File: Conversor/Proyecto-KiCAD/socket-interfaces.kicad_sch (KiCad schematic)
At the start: 24 parts, among them J10 DIMM100, P10 Header GPIO, P11 Header SD, P5 Header 7X2, P6 Header UART, P7 Header I2C, P8 Header PWM, P9 Header ADC, SW1 Switch, SW2 Switch, SW3 Switch, SW4 Switch

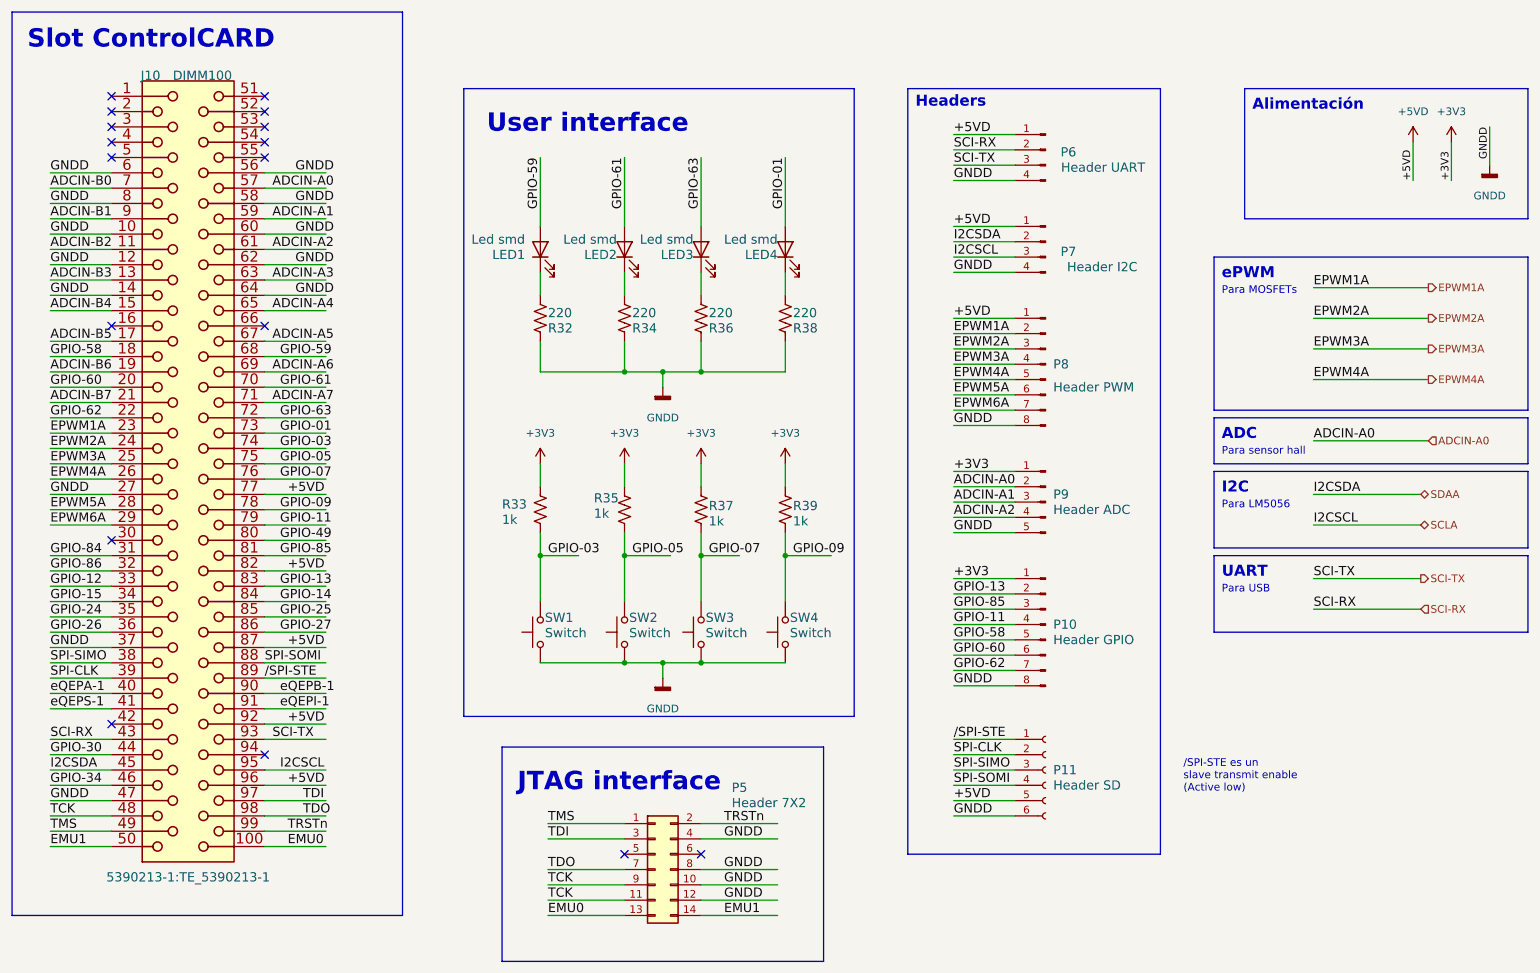
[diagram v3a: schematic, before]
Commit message: Arreglar los primeros dos items marcados por Jorge
- Usar EPWM1A/B y EPWM2A/B para poder usar la función de phase-shift de
los modulos PWM y ahorrarse la sincronización manual
- Agregar diodos de descarga D8 y D9 a la salida de los drivers
- Agregar el Technical Reference Manual del DSP a la bibliografía
(descripción ultra detallada de todas las funciones del DSP)
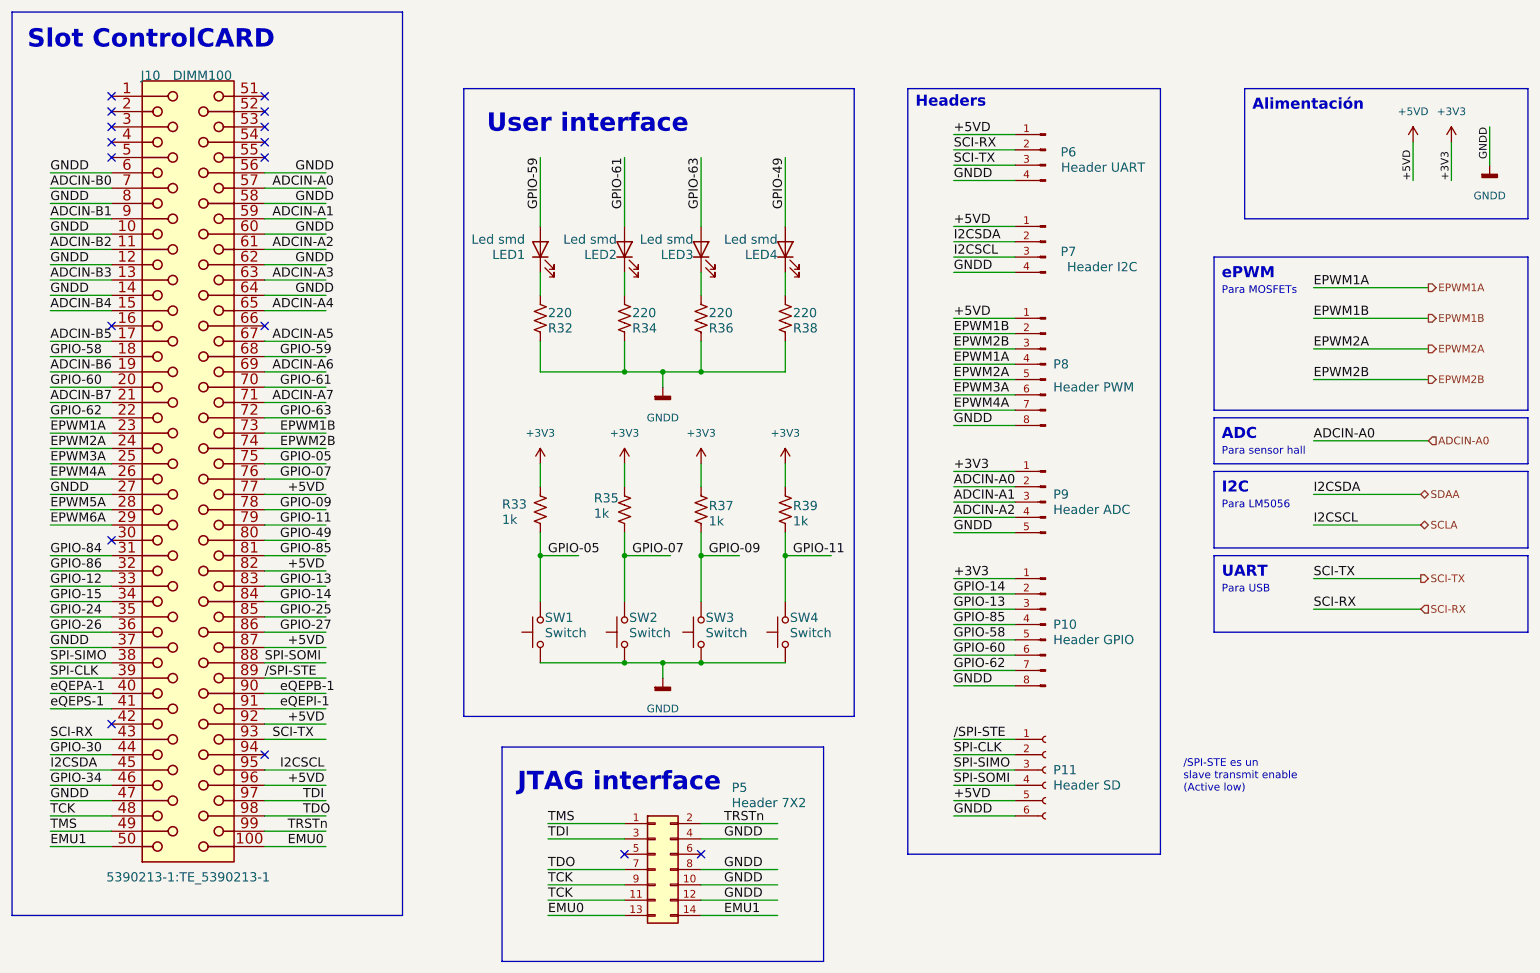
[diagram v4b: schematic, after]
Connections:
- net EPWM1A: now also P8.4 (Pin_4); no longer P8.2 (Pin_2)
- net EPWM2A: now also P8.5 (Pin_5); no longer P8.3 (Pin_3)
- net EPWM3A: now also P8.6 (Pin_6); no longer P8.4 (Pin_4)
- net EPWM4A: now also P8.7 (Pin_7); no longer P8.5 (Pin_5)
- net EPWM5A: no longer P8.6 (Pin_6)
- net EPWM6A: no longer P8.7 (Pin_7)
- net GPIO-05: now also R33.1, SW1.2; no longer R35.1, SW2.2
- net GPIO-07: now also R35.1, SW2.2; no longer R37.1, SW3.2
- net GPIO-09: now also R37.1, SW3.2; no longer R39.1, SW4.2
- net GPIO-11: now also R39.1, SW4.2; no longer P10.4 (Pin_4)
- net GPIO-13: now also P10.3 (Pin_3); no longer P10.2 (Pin_2)
- net GPIO-14: now also P10.2 (Pin_2)
- net GPIO-49: now also LED4.2 (A)
- net GPIO-85: now also P10.4 (Pin_4); no longer P10.3 (Pin_3)
- net GPIO-01 renamed EPWM1B
- net EPWM1B: now also P8.2 (Pin_2); no longer LED4.2 (A)
- removed net GPIO-03: J10.74 (p74), R33.1, SW1.2
- new net EPWM2B: J10.74 (p74), P8.3 (Pin_3)
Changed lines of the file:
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@@
     (effects (font (size 1.524 1.524)) (justify left bottom))
   )
-  (label "EPWM2A" (at 175.26 71.12 0)
-    (effects (font (size 1.524 1.524)) (justify left bottom))
-  )
-  (label "GPIO-11" (at 175.26 116.84 0)
+  (label "EPWM2B" (at 175.26 71.12 0)
+    (effects (font (size 1.524 1.524)) (justify left bottom))
+  )
+  (label "GPIO-85" (at 175.26 116.84 0)
     (effects (font (size 1.524 1.524)) (justify left bottom))
   )
@@
     (effects (font (size 1.524 1.524)) (justify left bottom))
   )
-  (label "EPWM5A" (at 175.26 78.74 0)
+  (label "EPWM3A" (at 175.26 78.74 0)
     (effects (font (size 1.524 1.524)) (justify left bottom))
   )
@@
     (effects (font (size 1.524 1.524)) (justify left bottom))
   )
-  (label "GPIO-85" (at 175.26 114.3 0)
+  (label "GPIO-13" (at 175.26 114.3 0)
     (effects (font (size 1.524 1.524)) (justify left bottom))
   )
@@
     (effects (font (size 1.524 1.524)) (justify left bottom))
   )
-  (label "EPWM6A" (at 175.26 81.28 0)
+  (label "EPWM4A" (at 175.26 81.28 0)
     (effects (font (size 1.524 1.524)) (justify left bottom))
   )
@@
     (effects (font (size 1.524 1.524)) (justify left bottom))
   )
-  (label "EPWM1A" (at 175.26 68.58 0)
+  (label "EPWM1B" (at 175.26 68.58 0)
     (effects (font (size 1.524 1.524)) (justify left bottom))
   )
@@
     (effects (font (size 1.524 1.524)) (justify left bottom))
   )
-  (label "GPIO-13" (at 175.26 111.76 0)
+  (label "GPIO-14" (at 175.26 111.76 0)
     (effects (font (size 1.524 1.524)) (justify left bottom))
   )
@@
     (effects (font (size 1.524 1.524)) (justify left bottom))
   )
-  (label "GPIO-05" (at 121.92 105.41 0)
+  (label "GPIO-07" (at 121.92 105.41 0)
     (effects (font (size 1.524 1.524)) (justify left bottom))
   )
@@
     (effects (font (size 1.524 1.524)) (justify left bottom))
   )
-  (label "EPWM3A" (at 175.26 73.66 0)
+  (label "EPWM1A" (at 175.26 73.66 0)
     (effects (font (size 1.524 1.524)) (justify left bottom))
   )
@@
     (effects (font (size 1.524 1.524)) (justify left bottom))
   )
-  (label "EPWM2A" (at 234.95 66.04 0)
+  (label "EPWM1B" (at 234.95 66.04 0)
     (effects (font (size 1.524 1.524)) (justify left bottom))
   )
@@
     (effects (font (size 1.524 1.524)) (justify left bottom))
   )
-  (label "GPIO-03" (at 107.95 105.41 0)
+  (label "GPIO-05" (at 107.95 105.41 0)
     (effects (font (size 1.524 1.524)) (justify left bottom))
   )
@@
     (effects (font (size 1.524 1.524)) (justify left bottom))
   )
-  (label "GPIO-03" (at 63.5 87.63 0)
+  (label "EPWM2B" (at 63.5 87.63 0)
     (effects (font (size 1.524 1.524)) (justify left bottom))
   )
@@
     (effects (font (size 1.524 1.524)) (justify left bottom))
   )
-  (label "EPWM3A" (at 234.95 71.12 0)
+  (label "EPWM2A" (at 234.95 71.12 0)
     (effects (font (size 1.524 1.524)) (justify left bottom))
   )
@@
     (effects (font (size 1.524 1.524)) (justify left bottom))
   )
-  (label "GPIO-01" (at 147.32 39.37 270)
+  (label "GPIO-49" (at 147.32 39.37 270)
     (effects (font (size 1.524 1.524)) (justify right bottom))
   )
@@
     (effects (font (size 1.524 1.524)) (justify left bottom))
   )
-  (label "EPWM4A" (at 234.95 76.2 0)
+  (label "EPWM2B" (at 234.95 76.2 0)
     (effects (font (size 1.524 1.524)) (justify left bottom))
   )
@@
     (effects (font (size 1.524 1.524)) (justify left bottom))
   )
-  (label "GPIO-01" (at 63.5 85.09 0)
+  (label "EPWM1B" (at 63.5 85.09 0)
     (effects (font (size 1.524 1.524)) (justify left bottom))
   )
@@
     (effects (font (size 1.524 1.524)) (justify left bottom))
   )
-  (label "EPWM4A" (at 175.26 76.2 0)
+  (label "EPWM2A" (at 175.26 76.2 0)
     (effects (font (size 1.524 1.524)) (justify left bottom))
   )
@@
     (effects (font (size 1.524 1.524)) (justify left bottom))
   )
-  (label "GPIO-09" (at 148.59 105.41 0)
+  (label "GPIO-11" (at 148.59 105.41 0)
     (effects (font (size 1.524 1.524)) (justify left bottom))
   )
@@
     (effects (font (size 1.524 1.524)) (justify left bottom))
   )
-  (label "GPIO-07" (at 134.62 105.41 0)
+  (label "GPIO-09" (at 134.62 105.41 0)
     (effects (font (size 1.524 1.524)) (justify left bottom))
   )
@@
     (effects (font (size 1.27 1.27)) (justify left))
   )
-  (hierarchical_label "EPWM3A" (shape output) (at 254 71.12 0)
+  (hierarchical_label "EPWM2A" (shape output) (at 254 71.12 0)
     (effects (font (size 1.27 1.27)) (justify left))
   )
@@
     (effects (font (size 1.27 1.27)) (justify left))
   )
-  (hierarchical_label "EPWM4A" (shape output) (at 254 76.2 0)
+  (hierarchical_label "EPWM2B" (shape output) (at 254 76.2 0)
     (effects (font (size 1.27 1.27)) (justify left))
   )
@@
     (effects (font (size 1.27 1.27)) (justify left))
   )
-  (hierarchical_label "EPWM2A" (shape output) (at 254 66.04 0)
-    (effects (font (size 1.27 1.27)) (justify left))
-  )
+  (hierarchical_label "EPWM1B" (shape output) (at 254 66.04 0)
+    (effects (font (size 1.27 1.27)) (justify left))
+  )
